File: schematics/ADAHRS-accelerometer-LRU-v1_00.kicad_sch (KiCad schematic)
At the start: 9 parts

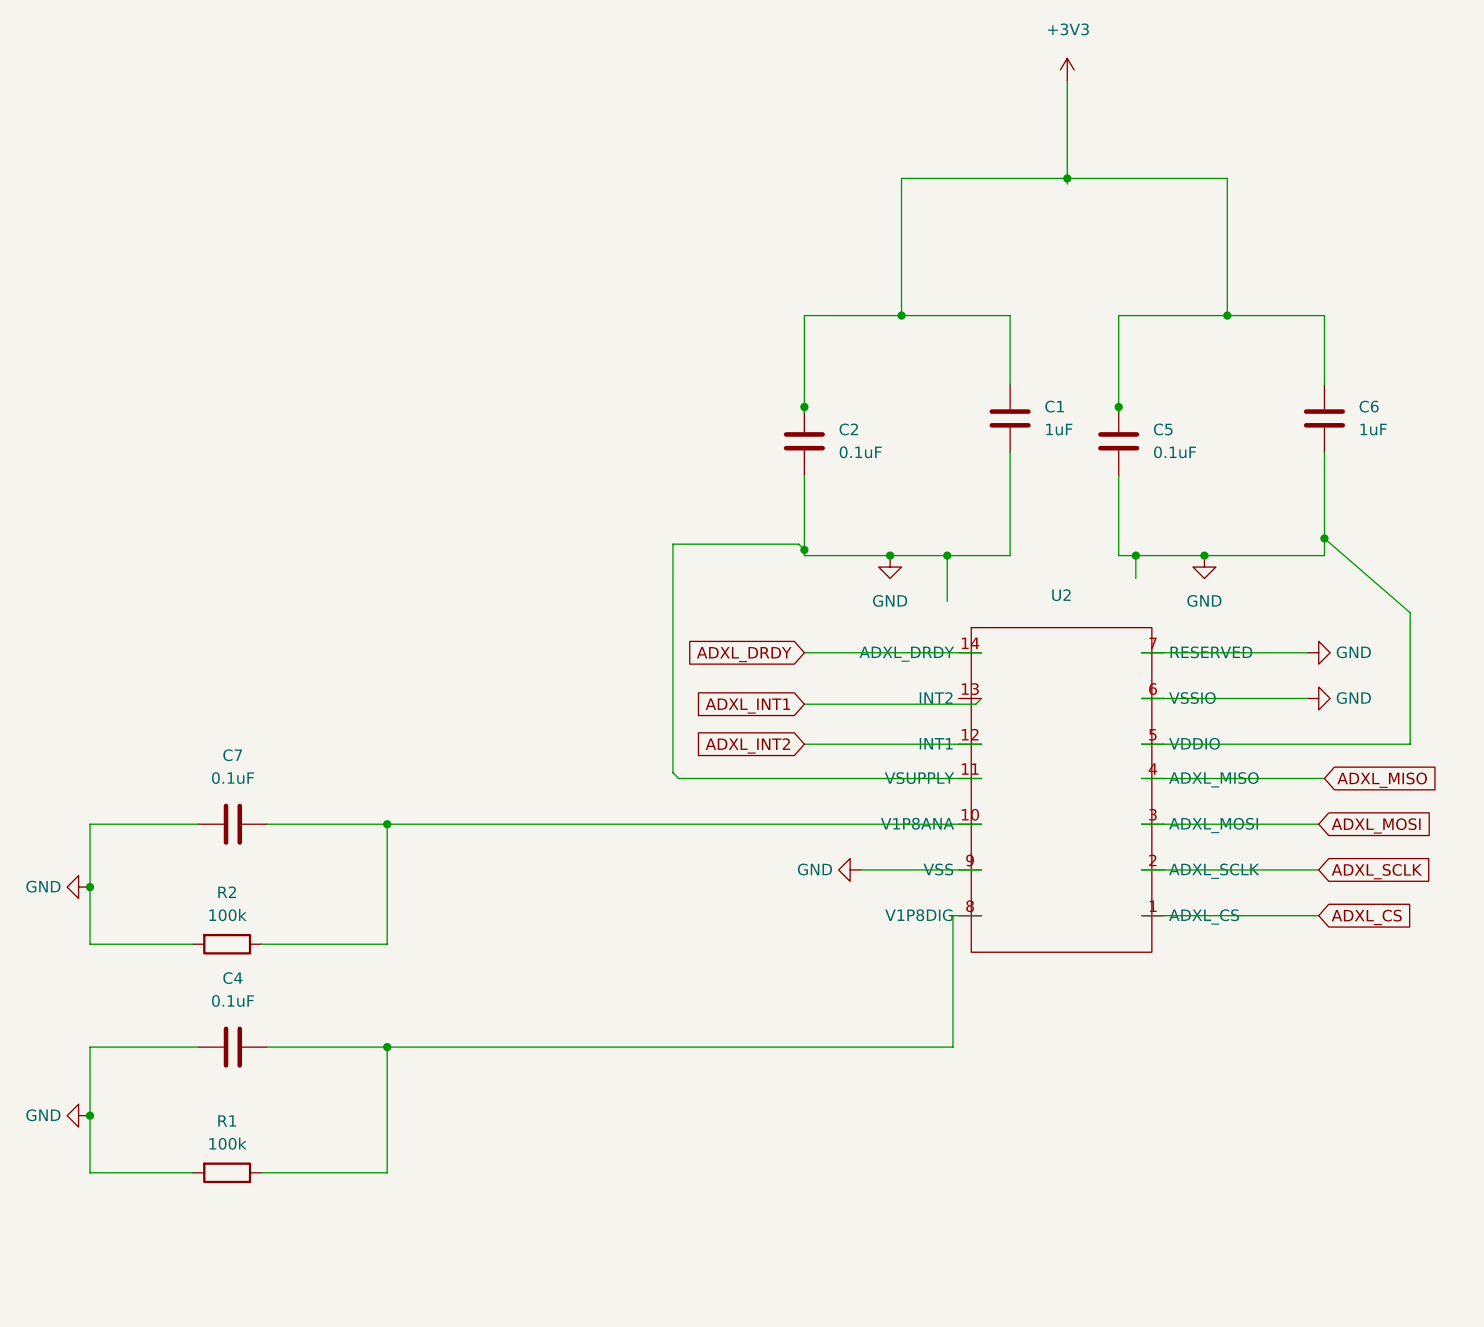
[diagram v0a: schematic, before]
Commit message: Re did the wiring structure v1.01
I need to rename the files. They do not track the true iterations
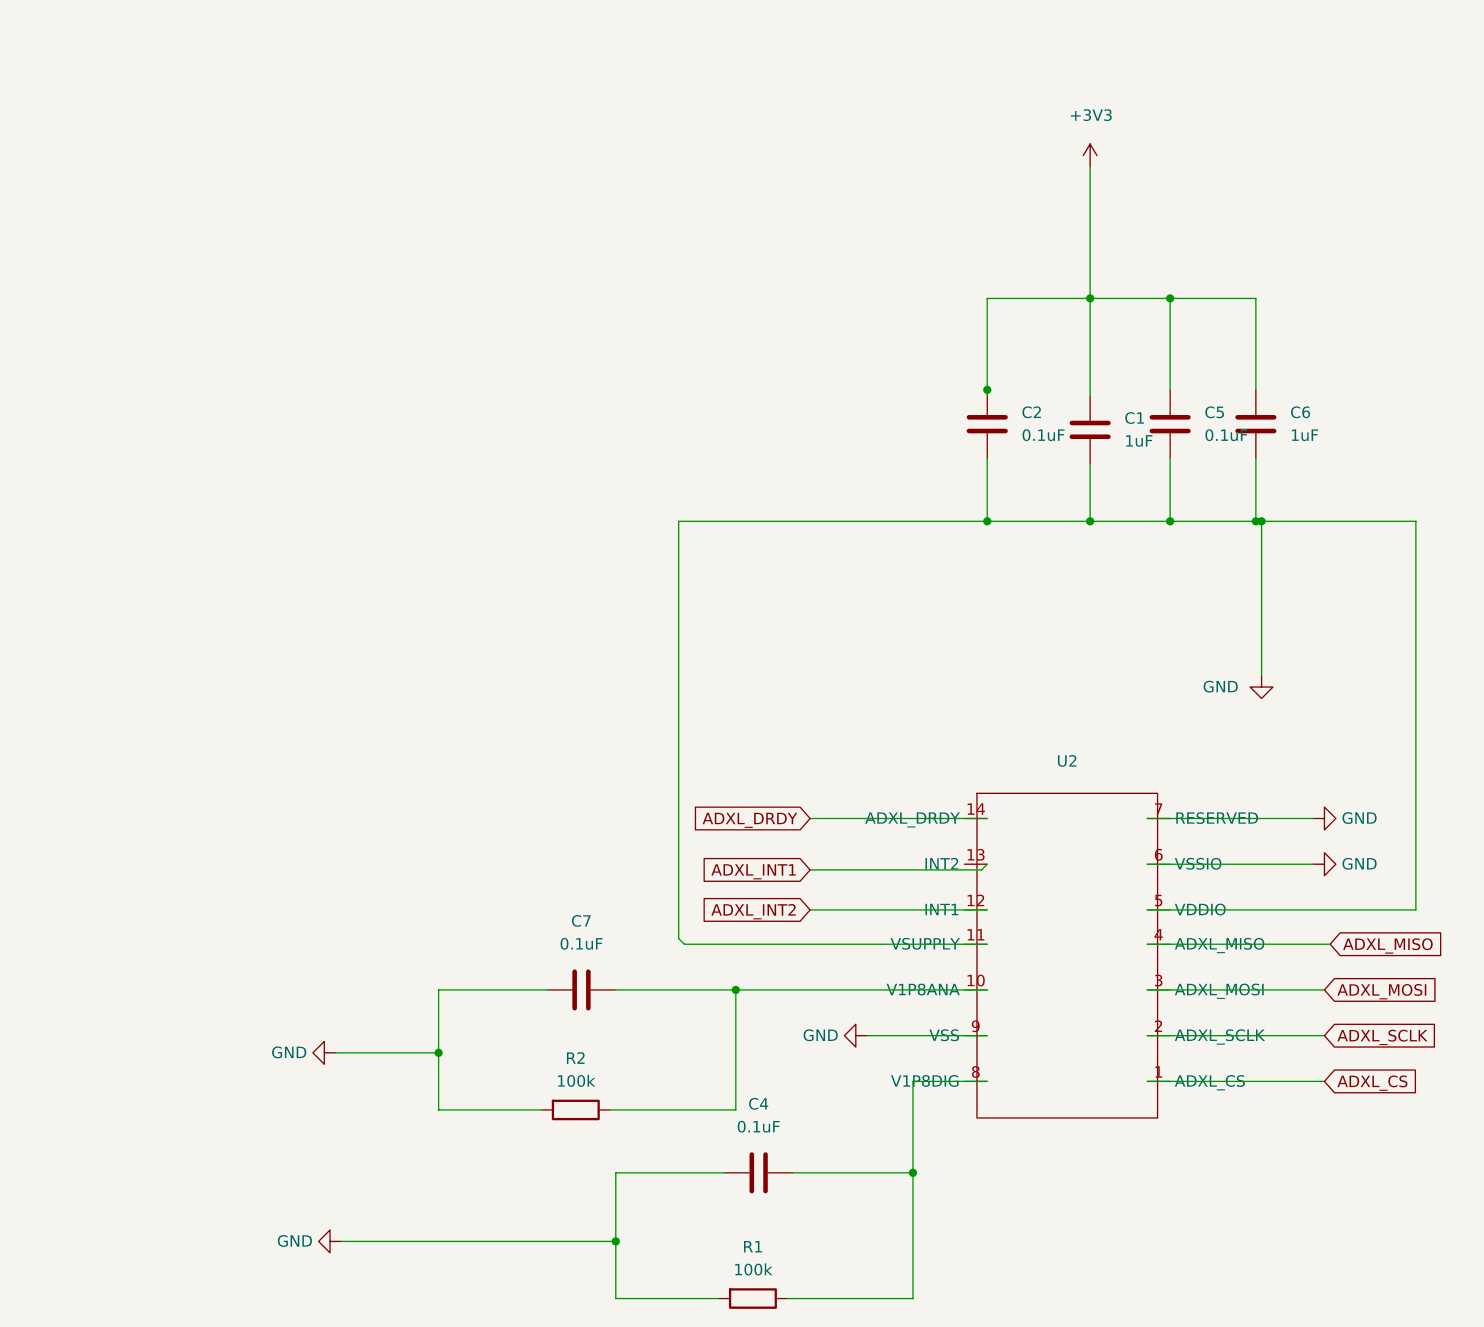
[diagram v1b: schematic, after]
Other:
- moved on the sheet: C1, C2, C4, C5, C6, C7, R1, R2, U2
